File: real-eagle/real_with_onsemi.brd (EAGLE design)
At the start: 104.1 x 123.4 mm, 49 parts, among them J2 POWER_JACK

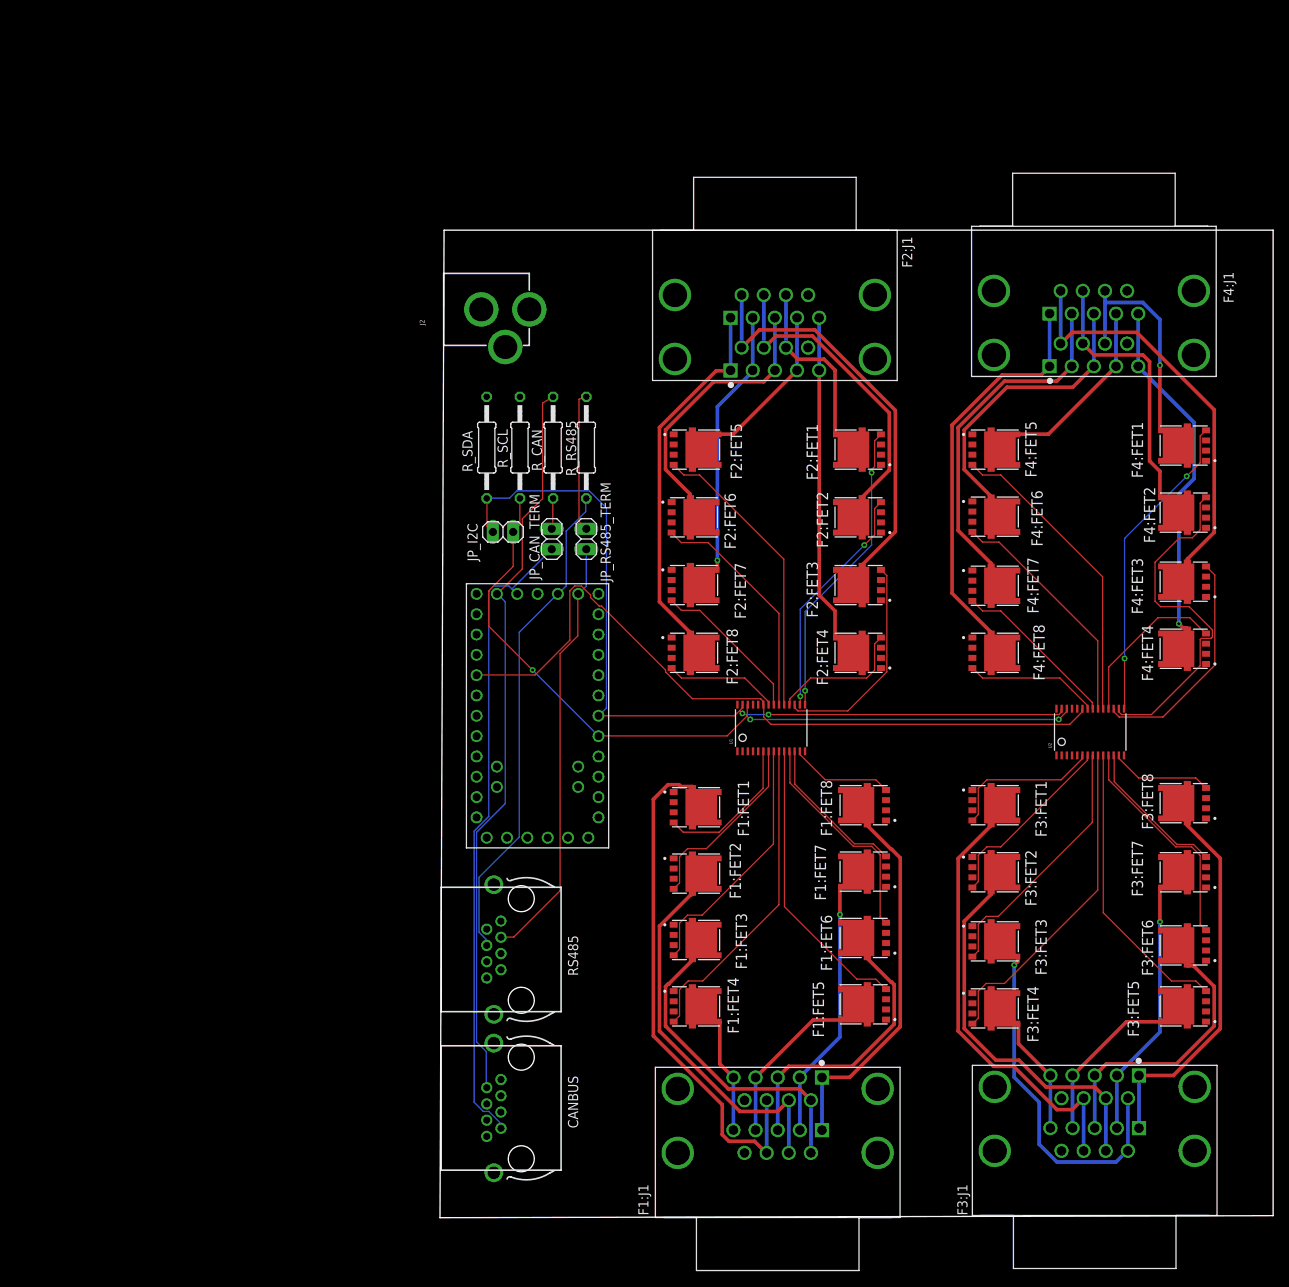
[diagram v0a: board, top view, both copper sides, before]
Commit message: Add modifications from @slacAdpai as of 2019/2/27
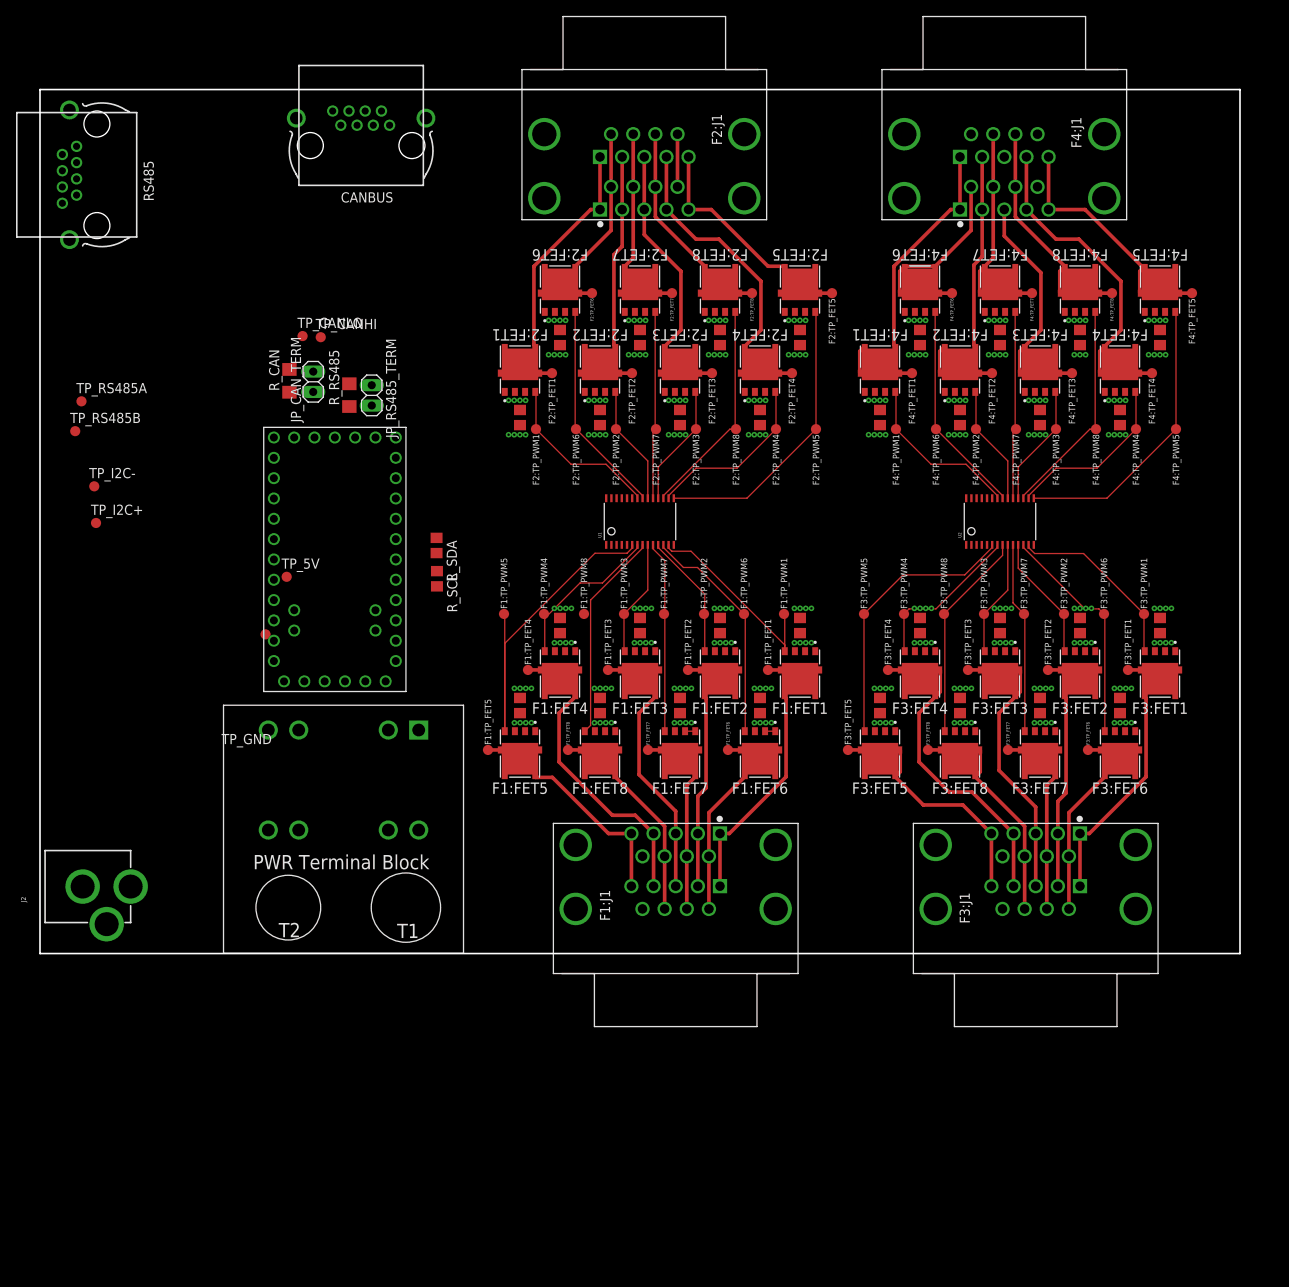
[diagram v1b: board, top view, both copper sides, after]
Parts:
- removed JP_I2C: (no value), pinhead:1X02
- added F1:C1, F1:C2, F1:C3, F1:C4, F1:C5, F1:C6, F1:C7, F1:C8, F2:C1, F2:C2, F2:C3, F2:C4, F2:C5, F2:C6, F2:C7, F2:C8, F3:C1, F3:C2, F3:C3, F3:C4, F3:C5, F3:C6, F3:C7, F3:C8, F4:C1, F4:C2, F4:C3, F4:C4, F4:C5, F4:C6, F4:C7, F4:C8: (no value), rcl:C0805
- added F1:TP_FET1, F1:TP_FET2, F1:TP_FET3, F1:TP_FET4, F1:TP_FET5, F1:TP_FET6, F1:TP_FET7, F1:TP_FET8, F1:TP_PWM1, F1:TP_PWM2, F1:TP_PWM3, F1:TP_PWM4, F1:TP_PWM5, F1:TP_PWM6, F1:TP_PWM7, F1:TP_PWM8, F2:TP_FET1, F2:TP_FET2, F2:TP_FET3, F2:TP_FET4, F2:TP_FET5, F2:TP_FET6, F2:TP_FET7, F2:TP_FET8, F2:TP_PWM1, F2:TP_PWM2, F2:TP_PWM3, F2:TP_PWM4, F2:TP_PWM5, F2:TP_PWM6, F2:TP_PWM7, F2:TP_PWM8, F3:TP_FET1, F3:TP_FET2, F3:TP_FET3, F3:TP_FET4, F3:TP_FET5, F3:TP_FET6, F3:TP_FET7, F3:TP_FET8, F3:TP_PWM1, F3:TP_PWM2, F3:TP_PWM3, F3:TP_PWM4, F3:TP_PWM5, F3:TP_PWM6, F3:TP_PWM7, F3:TP_PWM8, F4:TP_FET1, F4:TP_FET2, F4:TP_FET3, F4:TP_FET4, F4:TP_FET5, F4:TP_FET6, F4:TP_FET7, F4:TP_FET8, F4:TP_PWM1, F4:TP_PWM2, F4:TP_PWM3, F4:TP_PWM4, F4:TP_PWM5, F4:TP_PWM6, F4:TP_PWM7, F4:TP_PWM8, TP_5V, TP_CANHI, TP_CANLO, TP_GND, TP_I2C+, TP_I2C-, TP_RS485A, TP_RS485B: TPB1,27, testpad:B1,27
- added J_48V: PHOENIX_TERMINAL_BLOCK, real_library:TERMINAL_BLOCK_PHOENIX
- R_CAN, R_RS485: device rcl:0207/12 -> rcl:R1206
- R_SCL, R_SDA: value 4.7K -> 4.7k; device rcl:0207/12 -> rcl:R0805
- moved CANBUS 122.0 mm to (-9.86, 101.0), turned to 0 degrees
- moved RS485 110.4 mm to (-42.9, 97.3)
- moved J2 87.7 mm to (-52.4, 8.37)
- moved F1:FET5 53.2 mm to (10.0, 25.0), turned to 180 degrees
- moved F3:FET5 49.4 mm to (55.0, 25.0), turned to 180 degrees
- moved F4:FET8 46.6 mm to (80.0, 83.0), turned to 0 degrees
- moved F2:FET8 45.5 mm to (35.0, 83.0), turned to 0 degrees
- moved F1:FET4 44.9 mm to (15.0, 35.0), turned to 180 degrees
- moved F2:FET1 43.5 mm to (10.0, 73.0), turned to 0 degrees
- moved F3:FET4 42.9 mm to (60.0, 35.0), turned to 180 degrees
- moved F4:FET1 39.1 mm to (55.0, 73.0), turned to 0 degrees
- moved F2:FET7 37.6 mm to (25.0, 83.0), turned to 0 degrees
- moved F2:FET4 37.5 mm to (40.0, 73.0), turned to 0 degrees
- moved F2:FET2 37.2 mm to (20.0, 73.0), turned to 0 degrees
- moved F4:FET7 37.0 mm to (70.0, 83.0), turned to 0 degrees
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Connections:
- new net V_48V: F1:C1.1, F1:C2.1, F1:C3.1, F1:C4.1, F1:C5.1, F1:C6.1, F1:C7.1, F1:C8.1, F2:C1.1, F2:C2.1, F2:C3.1, F2:C4.1, F2:C5.1, F2:C6.1, F2:C7.1, F2:C8.1, F3:C1.1, F3:C2.1, F3:C3.1, F3:C4.1, F3:C5.1, F3:C6.1, F3:C7.1, F3:C8.1, F4:C1.1, F4:C2.1, F4:C3.1, F4:C4.1, F4:C5.1, F4:C6.1, F4:C7.1, F4:C8.1, J_48V.P$1, J_48V.P$2, J_48V.P$5, J_48V.P$6
- net GND: now also F1:C1.2, F1:C2.2, F1:C3.2, F1:C4.2, F1:C5.2, F1:C6.2, F1:C7.2, F1:C8.2, F2:C1.2, F2:C2.2, F2:C3.2, F2:C4.2, F2:C5.2, F2:C6.2, F2:C7.2, F2:C8.2, F3:C1.2, F3:C2.2, F3:C3.2, F3:C4.2, F3:C5.2, F3:C6.2, F3:C7.2, F3:C8.2, F4:C1.2, F4:C2.2, F4:C3.2, F4:C4.2, F4:C5.2, F4:C6.2, F4:C7.2, F4:C8.2, J_48V.P$3, J_48V.P$4, J_48V.P$7, J_48V.P$8, TP_GND.TP
- net HEATER_A0: now also F1:J1.A1, F1:J1.B1, F1:TP_FET1.TP; no longer F1:J1.A8, F1:J1.B8
- net HEATER_A1: now also F1:J1.A2, F1:J1.B2, F1:TP_FET2.TP; no longer F1:J1.A7, F1:J1.B7
- net HEATER_A2: now also F1:J1.A3, F1:J1.B3, F1:TP_FET3.TP; no longer F1:J1.A6, F1:J1.B6
- net HEATER_A3: now also F1:J1.A4, F1:J1.B4, F1:TP_FET4.TP; no longer F1:J1.A5, F1:J1.B5
- net HEATER_A4: now also F1:J1.A5, F1:J1.B5, F1:TP_FET5.TP; no longer F1:J1.A4, F1:J1.B4
- net HEATER_A5: now also F1:J1.A6, F1:J1.B6, F1:TP_FET6.TP; no longer F1:J1.A3, F1:J1.B3
- net HEATER_A6: now also F1:J1.A7, F1:J1.B7, F1:TP_FET7.TP; no longer F1:J1.A2, F1:J1.B2
- net HEATER_A7: now also F1:J1.A8, F1:J1.B8, F1:TP_FET8.TP; no longer F1:J1.A1, F1:J1.B1
- net HEATER_B0: now also F2:J1.A1, F2:J1.B1, F2:TP_FET1.TP; no longer F2:J1.A8, F2:J1.B8
- net HEATER_B1: now also F2:J1.A2, F2:J1.B2, F2:TP_FET2.TP; no longer F2:J1.A7, F2:J1.B7
- net HEATER_B2: now also F2:J1.A3, F2:J1.B3, F2:TP_FET3.TP; no longer F2:J1.A6, F2:J1.B6
- net HEATER_B3: now also F2:J1.A4, F2:J1.B4, F2:TP_FET4.TP; no longer F2:J1.A5, F2:J1.B5
- net HEATER_B4: now also F2:J1.A5, F2:J1.B5, F2:TP_FET5.TP; no longer F2:J1.A4, F2:J1.B4
- net HEATER_B5: now also F2:J1.A6, F2:J1.B6, F2:TP_FET6.TP; no longer F2:J1.A3, F2:J1.B3
- net HEATER_B6: now also F2:J1.A7, F2:J1.B7, F2:TP_FET7.TP; no longer F2:J1.A2, F2:J1.B2
- net HEATER_B7: now also F2:J1.A8, F2:J1.B8, F2:TP_FET8.TP; no longer F2:J1.A1, F2:J1.B1
- net HEATER_C0: now also F3:J1.A1, F3:J1.B1, F3:TP_FET1.TP; no longer F3:J1.A8, F3:J1.B8
- net HEATER_C1: now also F3:J1.A2, F3:J1.B2, F3:TP_FET2.TP; no longer F3:J1.A7, F3:J1.B7
- net HEATER_C2: now also F3:J1.A3, F3:J1.B3, F3:TP_FET3.TP; no longer F3:J1.A6, F3:J1.B6
- net HEATER_C3: now also F3:J1.A4, F3:J1.B4, F3:TP_FET4.TP; no longer F3:J1.A5, F3:J1.B5
- net HEATER_C4: now also F3:J1.A5, F3:J1.B5, F3:TP_FET5.TP; no longer F3:J1.A4, F3:J1.B4
- net HEATER_C5: now also F3:J1.A6, F3:J1.B6, F3:TP_FET6.TP; no longer F3:J1.A3, F3:J1.B3
- net HEATER_C6: now also F3:J1.A7, F3:J1.B7, F3:TP_FET7.TP; no longer F3:J1.A2, F3:J1.B2
- net HEATER_C7: now also F3:J1.A8, F3:J1.B8, F3:TP_FET8.TP; no longer F3:J1.A1, F3:J1.B1
- net HEATER_D0: now also F4:J1.A1, F4:J1.B1, F4:TP_FET1.TP; no longer F4:J1.A8, F4:J1.B8
- net HEATER_D1: now also F4:J1.A2, F4:J1.B2, F4:TP_FET2.TP; no longer F4:J1.A7, F4:J1.B7
- net HEATER_D2: now also F4:J1.A3, F4:J1.B3, F4:TP_FET3.TP; no longer F4:J1.A6, F4:J1.B6
- net HEATER_D3: now also F4:J1.A4, F4:J1.B4, F4:TP_FET4.TP; no longer F4:J1.A5, F4:J1.B5
- net HEATER_D4: now also F4:J1.A5, F4:J1.B5, F4:TP_FET5.TP; no longer F4:J1.A4, F4:J1.B4
- net HEATER_D5: now also F4:J1.A6, F4:J1.B6, F4:TP_FET6.TP; no longer F4:J1.A3, F4:J1.B3
- net HEATER_D6: now also F4:J1.A7, F4:J1.B7, F4:TP_FET7.TP; no longer F4:J1.A2, F4:J1.B2
- net HEATER_D7: now also F4:J1.A8, F4:J1.B8, F4:TP_FET8.TP; no longer F4:J1.A1, F4:J1.B1
- net N$1: now also R_CAN.1, TP_CANLO.TP; no longer R_CAN.2
- net N$16: no longer JP_I2C.2
- net N$19: no longer JP_I2C.1
- net N$3: now also TP_CANHI.TP
- net N$4: now also R_CAN.2; no longer R_CAN.1
- net PWM_A0: now also F1:FET5.4, F1:TP_PWM5.TP; no longer F1:FET1.4
- net PWM_A1: now also F1:FET4.4, F1:TP_PWM4.TP; no longer F1:FET2.4
- net PWM_A2: now also F1:FET8.4, F1:TP_PWM8.TP; no longer F1:FET3.4
- net PWM_A3: now also F1:FET3.4, F1:TP_PWM3.TP; no longer F1:FET4.4
- net PWM_A4: now also F1:FET7.4, F1:TP_PWM7.TP; no longer F1:FET5.4
- net PWM_A5: now also F1:FET2.4, F1:TP_PWM2.TP; no longer F1:FET6.4
- net PWM_A6: now also F1:FET6.4, F1:TP_PWM6.TP; no longer F1:FET7.4
- net PWM_A7: now also F1:FET1.4, F1:TP_PWM1.TP; no longer F1:FET8.4
- net PWM_B0: now also F2:FET5.4, F2:TP_PWM5.TP; no longer F2:FET1.4
- net PWM_B1: now also F2:FET4.4, F2:TP_PWM4.TP; no longer F2:FET2.4
- net PWM_B2: now also F2:FET8.4, F2:TP_PWM8.TP; no longer F2:FET3.4
- net PWM_B3: now also F2:FET3.4, F2:TP_PWM3.TP; no longer F2:FET4.4
- net PWM_B4: now also F2:FET7.4, F2:TP_PWM7.TP; no longer F2:FET5.4
- net PWM_B5: now also F2:FET2.4, F2:TP_PWM2.TP; no longer F2:FET6.4
- net PWM_B6: now also F2:FET6.4, F2:TP_PWM6.TP; no longer F2:FET7.4
- net PWM_B7: now also F2:FET1.4, F2:TP_PWM1.TP; no longer F2:FET8.4
- net PWM_C0: now also F3:FET5.4, F3:TP_PWM5.TP; no longer F3:FET1.4
- net PWM_C1: now also F3:FET4.4, F3:TP_PWM4.TP; no longer F3:FET2.4
- net PWM_C2: now also F3:FET8.4, F3:TP_PWM8.TP; no longer F3:FET3.4
- net PWM_C3: now also F3:FET3.4, F3:TP_PWM3.TP; no longer F3:FET4.4
- net PWM_C4: now also F3:FET7.4, F3:TP_PWM7.TP; no longer F3:FET5.4
- net PWM_C5: now also F3:FET2.4, F3:TP_PWM2.TP; no longer F3:FET6.4
- net PWM_C6: now also F3:FET6.4, F3:TP_PWM6.TP; no longer F3:FET7.4
- net PWM_C7: now also F3:FET1.4, F3:TP_PWM1.TP; no longer F3:FET8.4
- net PWM_D0: now also F4:FET5.4, F4:TP_PWM5.TP; no longer F4:FET1.4
- net PWM_D1: now also F4:FET4.4, F4:TP_PWM4.TP; no longer F4:FET2.4
- net PWM_D2: now also F4:FET8.4, F4:TP_PWM8.TP; no longer F4:FET3.4
- net PWM_D3: now also F4:FET3.4, F4:TP_PWM3.TP; no longer F4:FET4.4
- net PWM_D4: now also F4:FET7.4, F4:TP_PWM7.TP; no longer F4:FET5.4
- net PWM_D5: now also F4:FET2.4, F4:TP_PWM2.TP; no longer F4:FET6.4
- net PWM_D6: now also F4:FET6.4, F4:TP_PWM6.TP; no longer F4:FET7.4
- net PWM_D7: now also F4:FET1.4, F4:TP_PWM1.TP; no longer F4:FET8.4
- net VCC: now also TP_5V.TP
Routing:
- net N$19: track 106.9 -> 0.00 mm, vias 2 -> 0
- net N$16: track 99.0 -> 0.00 mm, vias 3 -> 0
- net ENABLE: track 93.6 -> 0.00 mm
- net N$4: track 92.0 -> 0.00 mm
- net N$3: track 81.0 -> 0.00 mm
- net N$5: track 61.9 -> 0.00 mm
- net N$7: track 53.9 -> 0.00 mm
- net HEATER_A0: track 64.3 -> 29.3 mm
- net HEATER_C3: track 14.8 -> 45.2 mm
- net PWM_A0: track 18.6 -> 46.9 mm
- net PWM_C3: track 41.4 -> 14.6 mm
- net PWM_A3: track 40.3 -> 14.6 mm
- net HEATER_B7: track 45.7 -> 20.5 mm
- net HEATER_A7: track 45.9 -> 20.9 mm
- net HEATER_C0: track 54.3 -> 29.3 mm
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- added copper zone on layer 2, net GND
- added copper zone on layer 15, net V_48V
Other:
- board size 104.1 x 123.4 mm -> 150 x 108 mm
